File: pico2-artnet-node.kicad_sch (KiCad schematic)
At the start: 15 parts, among them J6 USB_C_Receptacle_PowerOnly_6P, U1 W5500-EVB-PICO2, U6 WIZPoE Hat, U8 AMS1117-3.3

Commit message: v0.2 new DMX circuitry
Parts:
- removed JP1: disable onboard LDO, Jumper:SolderJumper-2_P1.3mm_Open_RoundedPad1.0x1.5mm, symbol Jumper:Jumper_2_Bridged
- removed JP2: disable onboard LDO, Connector_PinSocket_2.54mm:PinSocket_1x02_P2.54mm_Vertical, symbol Jumper:Jumper_2_Bridged
- added C5, C8: 10u, Capacitor_SMD:C_0603_1608Metric, symbol Device:C_Small
- added C6, C7: 0.1u, Capacitor_SMD:C_0603_1608Metric, symbol Device:C_Small
- added U4: B0505S-2WR3, EasyEDA:PWRM-TH_BXXXXS-2WR3, symbol impart EasyEDA:B0505S-2WR3_C5369473
- C1: renamed from C3; LCSC Part C96446 -> C19702
- C4: LCSC Part C96446 -> C19702
- renumbered C1 to C3, D9 to D1, D10 to D2, D11 to D3, J6 to J1, U6 to U1, U1 to U2, U8 to U3
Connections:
- net +5V: now also C5.2, C6.2, U4.1 (+VIN)
- net GND: now also U2.37 (3V3_EN), C5.1, C6.1, U4.2 (GND)
- new net +5VA: C7.1, C8.1, U4.6 (+Vo)
- new net GNDA: C7.2, C8.2, U4.4 (-Vo)
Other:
- sheet DMX 1 ports: added +5V ISO, GND ISO; removed +5V, GND
- sheet DMX 2 ports: added +5V ISO, GND ISO; removed +5V, GND
- sheet DMX 3 ports: added +5V ISO, GND ISO; removed +5V, GND
- sheet DMX 4 ports: added +5V ISO, GND ISO; removed +5V, GND

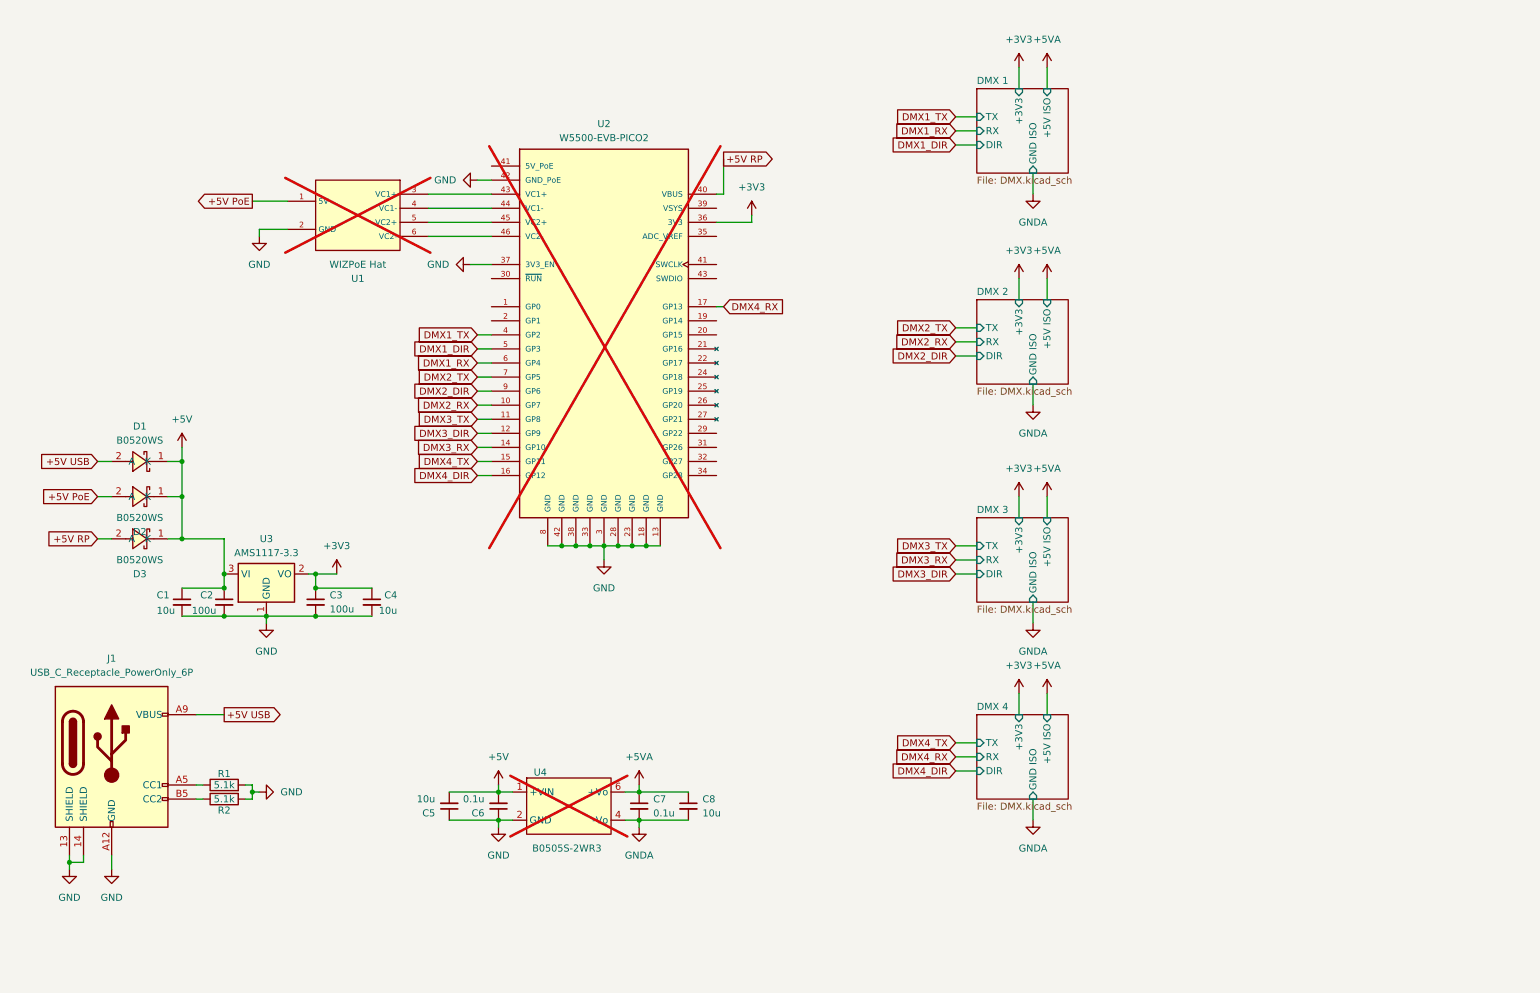
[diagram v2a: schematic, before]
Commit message: add levelshifter and silkscreen
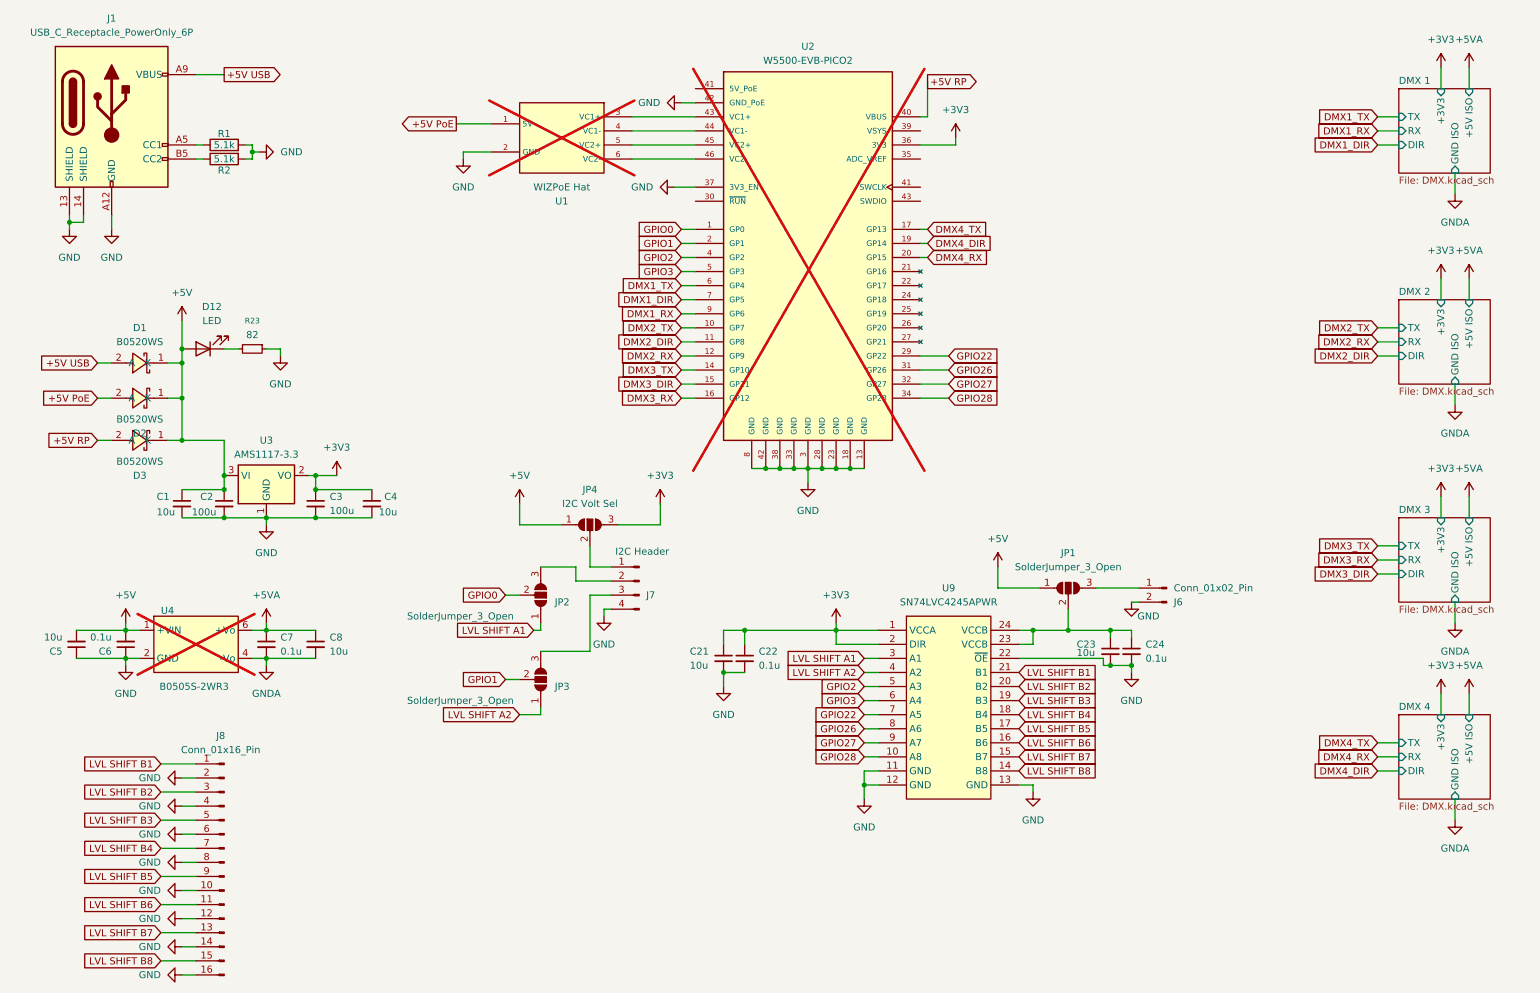
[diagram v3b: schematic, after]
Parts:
- added C21, C23: 10u, Capacitor_SMD:C_0603_1608Metric, symbol Device:C_Small
- added C22, C24: 0.1u, Capacitor_SMD:C_0603_1608Metric, symbol Device:C_Small
- added D12: LED, LED_SMD:LED_0805_2012Metric, symbol Device:LED
- added J6: Conn_01x02_Pin, Connector_PinSocket_2.54mm:PinSocket_1x02_P2.54mm_Vertical, symbol Connector:Conn_01x02_Pin
- added J7: I2C Header, Connector_PinSocket_2.54mm:PinSocket_1x04_P2.54mm_Vertical, symbol Connector:Conn_01x04_Pin
- added J8: Conn_01x16_Pin, Connector_PinSocket_2.54mm:PinSocket_1x16_P2.54mm_Vertical, symbol Connector:Conn_01x16_Pin
- added JP1, JP2, JP3: SolderJumper_3_Open, Jumper:SolderJumper-3_P1.3mm_Open_RoundedPad1.0x1.5mm, symbol Jumper:SolderJumper_3_Open
- added JP4: I2C Volt Sel, Jumper:SolderJumper-3_P1.3mm_Open_RoundedPad1.0x1.5mm, symbol Jumper:SolderJumper_3_Open
- added R23: 82, Resistor_SMD:R_0603_1608Metric, symbol Device:R_Small
- added U9: SN74LVC4245APWR, EasyEDA:TSSOP-24_L7.8-W4.4-P0.65-LS6.4-BL, symbol impart EasyEDA:SN74LVC4245APWR
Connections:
- net +3V3: now also C21.1, C22.1, JP4.3 (B), U9.1 (VCCA), U9.2 (DIR)
- net +5V: now also D12.2 (A), JP1.1 (A), JP4.1 (A)
- net DMX1_DIR: now also U2.7 (GP5); no longer U2.5 (GP3)
- net DMX1_RX: now also U2.9 (GP6); no longer U2.6 (GP4)
- net DMX1_TX: now also U2.6 (GP4); no longer U2.4 (GP2)
- net DMX2_DIR: now also U2.11 (GP8); no longer U2.9 (GP6)
- net DMX2_RX: now also U2.12 (GP9); no longer U2.10 (GP7)
- net DMX2_TX: now also U2.10 (GP7); no longer U2.7 (GP5)
- net DMX3_DIR: now also U2.15 (GP11); no longer U2.12 (GP9)
- net DMX3_RX: now also U2.16 (GP12); no longer U2.14 (GP10)
- net DMX3_TX: now also U2.14 (GP10); no longer U2.11 (GP8)
- net DMX4_DIR: now also U2.19 (GP14); no longer U2.16 (GP12)
- net DMX4_RX: now also U2.20 (GP15); no longer U2.17 (GP13)
- net DMX4_TX: now also U2.17 (GP13); no longer U2.15 (GP11)
- net GND: now also C21.2, C22.2, C23.2, C24.2, J6.2 (Pin_2), J7.4 (Pin_4), J8.10 (Pin_10), J8.12 (Pin_12), J8.14 (Pin_14), J8.16 (Pin_16), J8.2 (Pin_2), J8.4 (Pin_4), J8.6 (Pin_6), J8.8 (Pin_8), R23.1, U9.11 (GND), U9.12 (GND), U9.13 (GND), U9.22 (~{OE})
- net GPIO0: now reaches U2.1 (GP0)
- net GPIO0: now also JP2.2 (C)
- net GPIO1: now reaches U2.2 (GP1)
- net GPIO1: now also JP3.2 (C)
- net GPIO22: now reaches U2.29 (GP22)
- net GPIO22: now also U9.7 (A5)
- net GPIO26: now reaches U2.31 (GP26)
- net GPIO26: now also U9.8 (A6)
- net GPIO27: now reaches U2.32 (GP27)
- net GPIO27: now also U9.9 (A7)
- net GPIO28: now reaches U2.34 (GP28)
- net GPIO28: now also U9.10 (A8)
- new net: C23.1, C24.1, JP1.2 (C), U9.23 (VCCB), U9.24 (VCCB)
- new net: J7.1 (Pin_1), JP4.2 (C)
- new net: J7.2 (Pin_2), JP2.3 (B)
- new net: J7.3 (Pin_3), JP3.3 (B)
- new net: D12.1 (K), R23.2
- new net: J6.1 (Pin_1), JP1.3 (B)
- new net GPIO2: U2.4 (GP2), U9.5 (A3)
- new net GPIO3: U2.5 (GP3), U9.6 (A4)
- new net LVL SHIFT A1: JP2.1 (A), U9.3 (A1)
- new net LVL SHIFT A2: JP3.1 (A), U9.4 (A2)
- new net LVL SHIFT B1: J8.1 (Pin_1), U9.21 (B1)
- new net LVL SHIFT B2: J8.3 (Pin_3), U9.20 (B2)
- new net LVL SHIFT B3: J8.5 (Pin_5), U9.19 (B3)
- new net LVL SHIFT B4: J8.7 (Pin_7), U9.18 (B4)
- new net LVL SHIFT B5: J8.9 (Pin_9), U9.17 (B5)
- new net LVL SHIFT B6: J8.11 (Pin_11), U9.16 (B6)
- new net LVL SHIFT B7: J8.13 (Pin_13), U9.15 (B7)
- new net LVL SHIFT B8: J8.15 (Pin_15), U9.14 (B8)
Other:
- moved on the sheet: C1, C2, C3, C4, C5, C6, C7, C8, D1, D2, D3, J1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

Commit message: change solder jumpers to pins & power break out
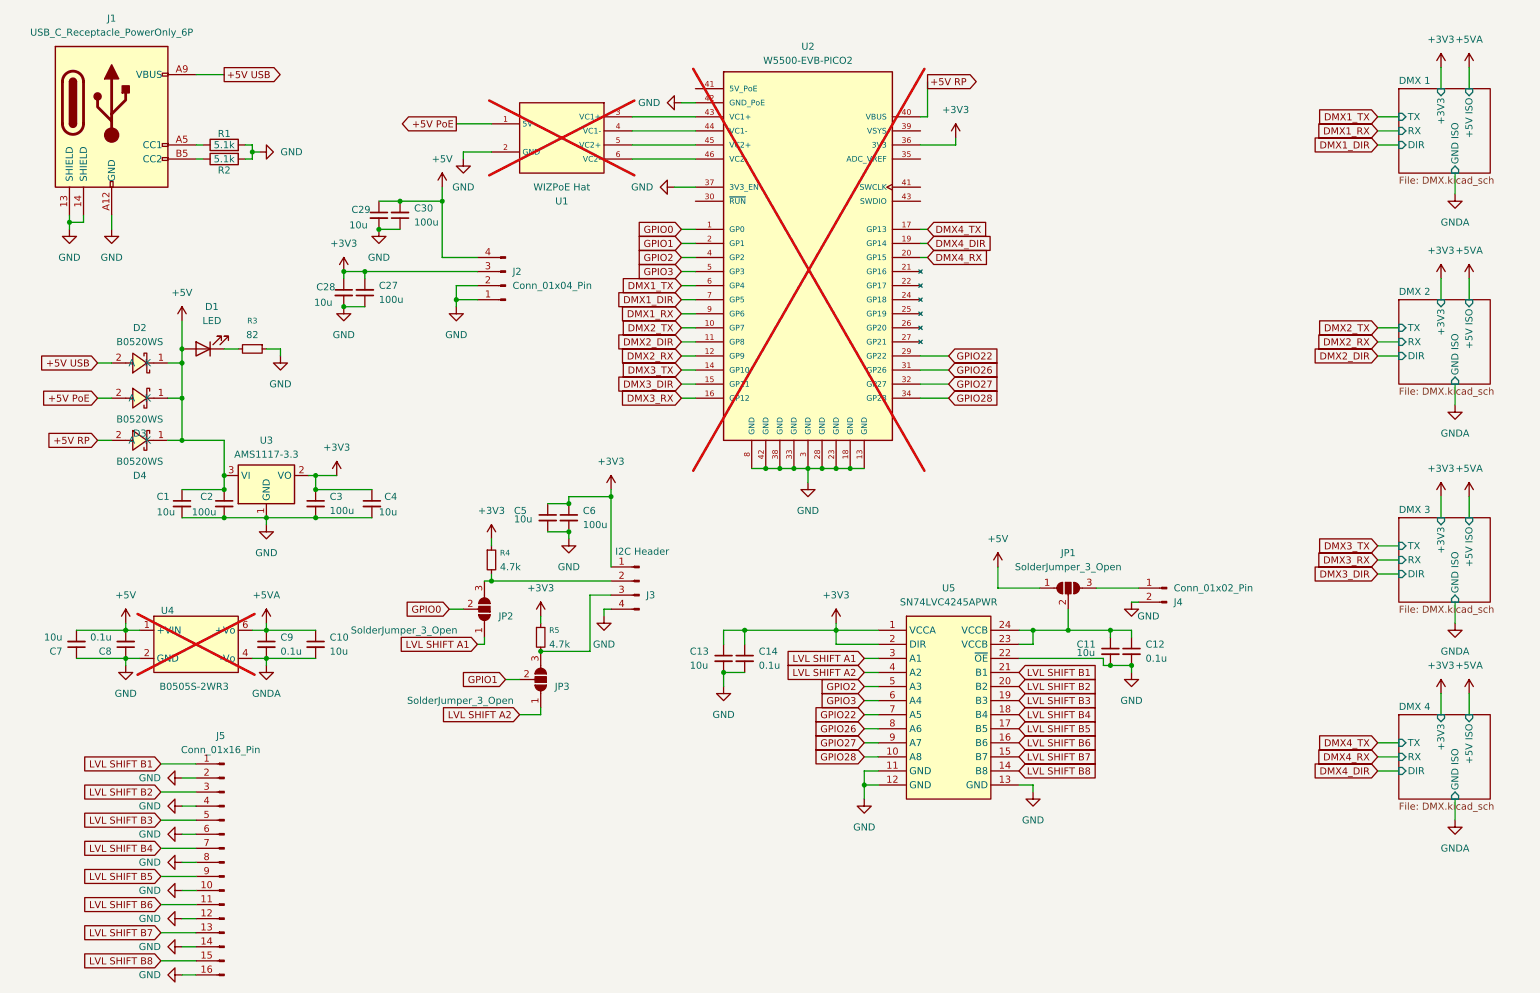
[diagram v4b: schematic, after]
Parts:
- removed JP4: I2C Volt Sel, Jumper:SolderJumper-3_P1.3mm_Open_RoundedPad1.0x1.5mm, symbol Jumper:SolderJumper_3_Open
- added C27, C30, C6: 100u, Capacitor_SMD:C_1206_3216Metric, symbol Device:C_Small
- added C28, C29, C5: 10u, Capacitor_SMD:C_0603_1608Metric, symbol Device:C_Small
- added J2: Conn_01x04_Pin, Connector:FanPinHeader_1x04_P2.54mm_Vertical, symbol Connector:Conn_01x04_Pin
- added R4, R5: 4.7k, Resistor_SMD:R_0603_1608Metric, symbol Device:R_Small
- J3: renamed from J7; footprint Connector_PinSocket_2.54mm:PinSocket_1x04_P2.54mm_Vertical -> Connector:FanPinHeader_1x04_P2.54mm_Vertical
- JP1, JP2, JP3: footprint Jumper:SolderJumper-3_P1.3mm_Open_RoundedPad1.0x1.5mm -> Connector_PinHeader_2.54mm:PinHeader_1x03_P2.54mm_Vertical
- renumbered C8 to C10, C23 to C11, C24 to C12, C21 to C13, C22 to C14, C5 to C7, C6 to C8, C7 to C9, D12 to D1, D1 to D2, D2 to D3, D3 to D4, J6 to J4, J8 to J5, R23 to R3, U9 to U5
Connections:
- net +3V3: now also J3.1 (Pin_1), C27.2, C28.1, C5.1, C6.1, J2.3 (Pin_3), R4.1, R5.1
- net +5V: now also C29.1, C30.2, J2.4 (Pin_4)
- net GND: now also C27.1, C28.2, C29.2, C30.1, C5.2, C6.2, J2.1 (Pin_1), J2.2 (Pin_2)
- net at J3.2 (Pin_2), JP2.3 (B): now also R4.2
- net at J3.3 (Pin_3), JP3.3 (B): now also R5.2
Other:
- moved on the sheet: JP2

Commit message: remove PoE Breakout & rund DRC
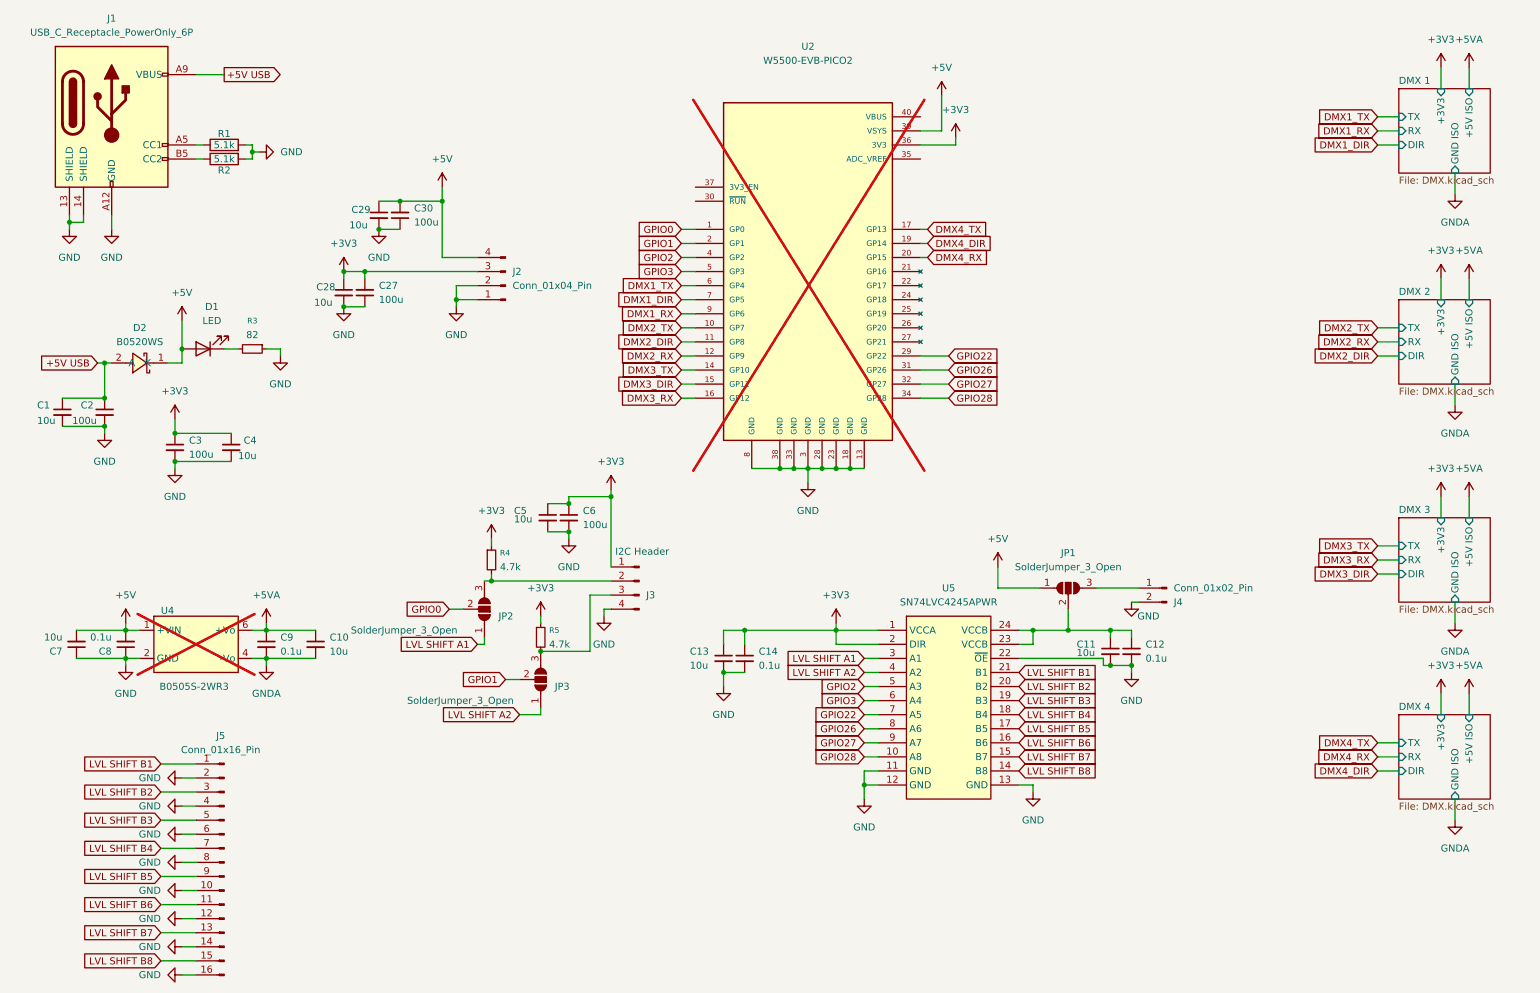
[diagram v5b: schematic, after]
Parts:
- removed D3, D4: B0520WS, EasyEDA:SOD-323_L1.7-W1.3-LS2.6-RD-1, symbol impart EasyEDA:B0520WS_C7502696
- removed U1: WIZPoE Hat, W5500-EVB-PICO:WIZPoE Hat, symbol W5500-EVB-PICO:Wiznet_PoE_Hat
- removed U3: AMS1117-3.3, Package_TO_SOT_SMD:SOT-223-3_TabPin2, symbol Regulator_Linear:AMS1117-3.3
- J1: footprint EasyEDA:USB-C-SMD_YPE-C-6PWTL-10-0108 -> EasyEDA:USB-C-SMD_YPE-C-6PWTL-10-0108_Board-overhang
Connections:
- net +5V: now also U2.39 (VSYS); no longer C1.1, C2.1
- net +5V USB: now also C1.1, C2.1
- net GND: no longer U2.37 (3V3_EN), U2.42 (GND_PoE)
- net +5V RP: no longer names the net of U2.40 (VBUS)
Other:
- moved on the sheet: C1, C2, C3, C4
